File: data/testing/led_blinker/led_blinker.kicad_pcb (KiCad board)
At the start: 2 copper layers, 20 x 25 mm, 7 parts, among them U1 ATtiny85

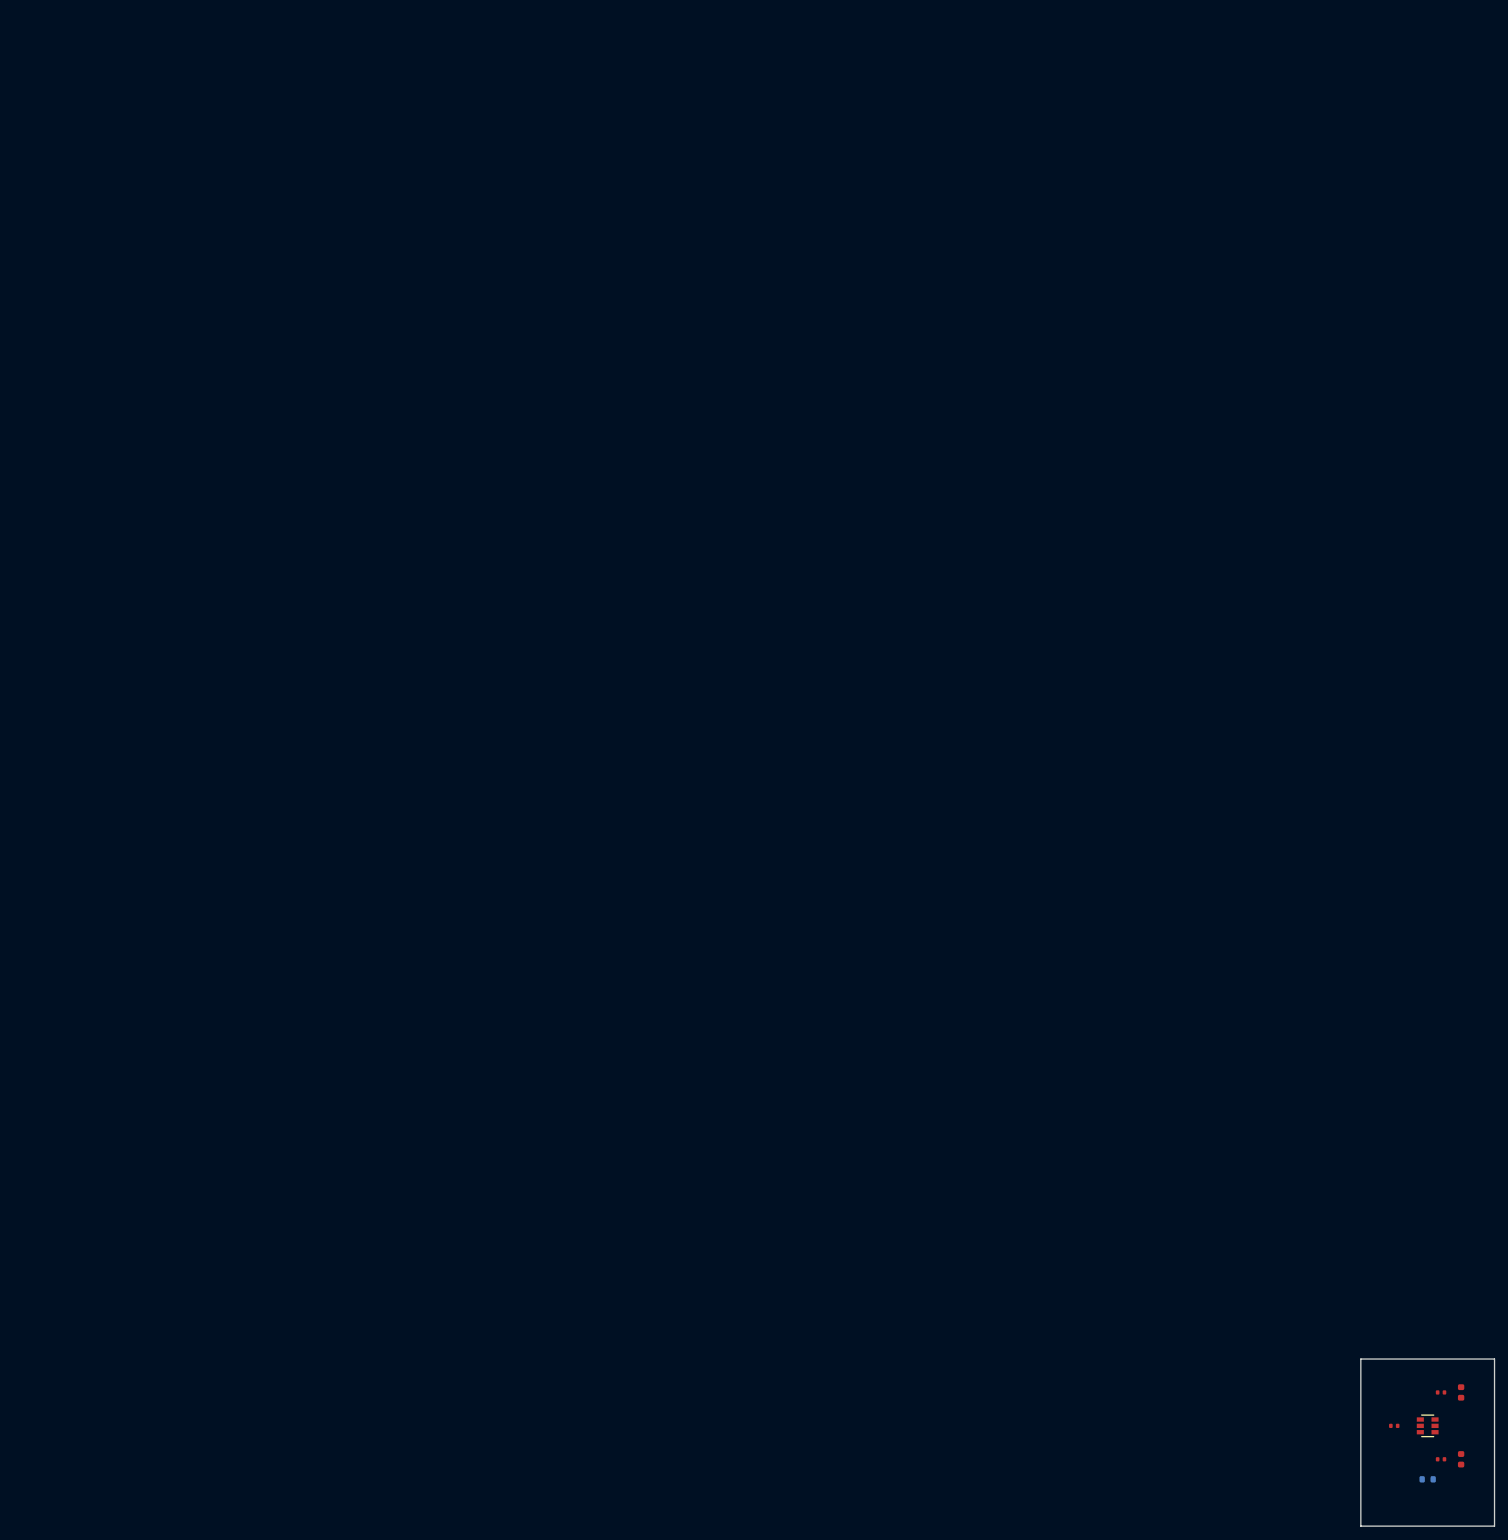
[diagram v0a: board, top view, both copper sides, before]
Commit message: chore(data): led_blinker.kicad_pcbに銅箔接続を追加
つながった銅箔ポリゴン抽出機能のテスト材料として、各ネットを
パッド間トラックで結線。R3 (B_Cu) はビアを介してF_Cu側と接続。

Co-Authored-By: Claude Opus 4.7 (1M context) <noreply@anthropic.com>
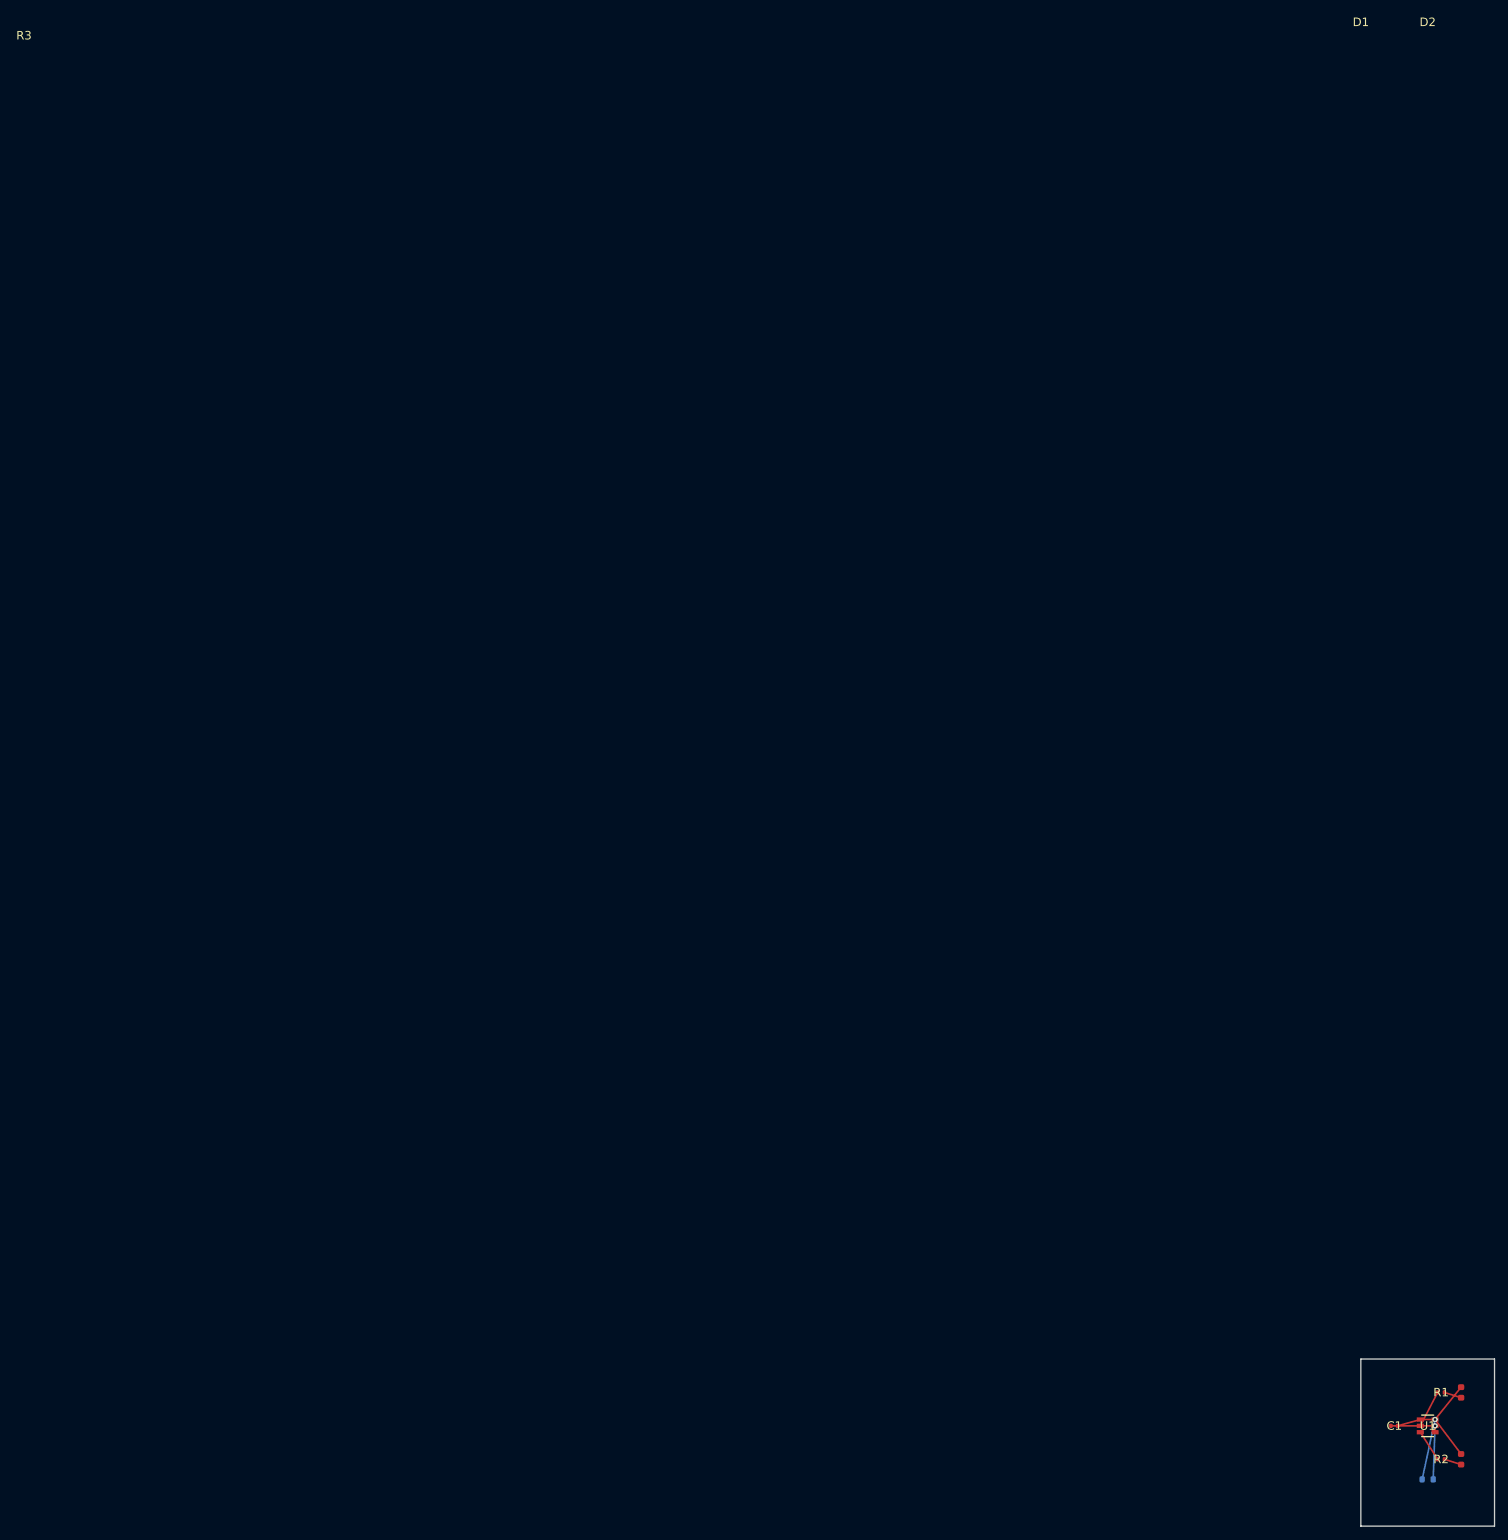
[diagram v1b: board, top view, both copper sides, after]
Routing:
- net GND: track 0.00 -> 27.6 mm, vias 0 -> 1
- net VCC: track 0.00 -> 15.6 mm, vias 0 -> 1
- net LED1: track 0.00 -> 8.24 mm
- net LED2: track 0.00 -> 7.42 mm
